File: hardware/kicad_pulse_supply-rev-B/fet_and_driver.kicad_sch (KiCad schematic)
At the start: 53 parts, among them J2 SIG_EXT, Q1 GAN7R0-150LBE, U1 UCC27611DRVT, U4 MAX4378, U6 MCP1703T-5002E/MB

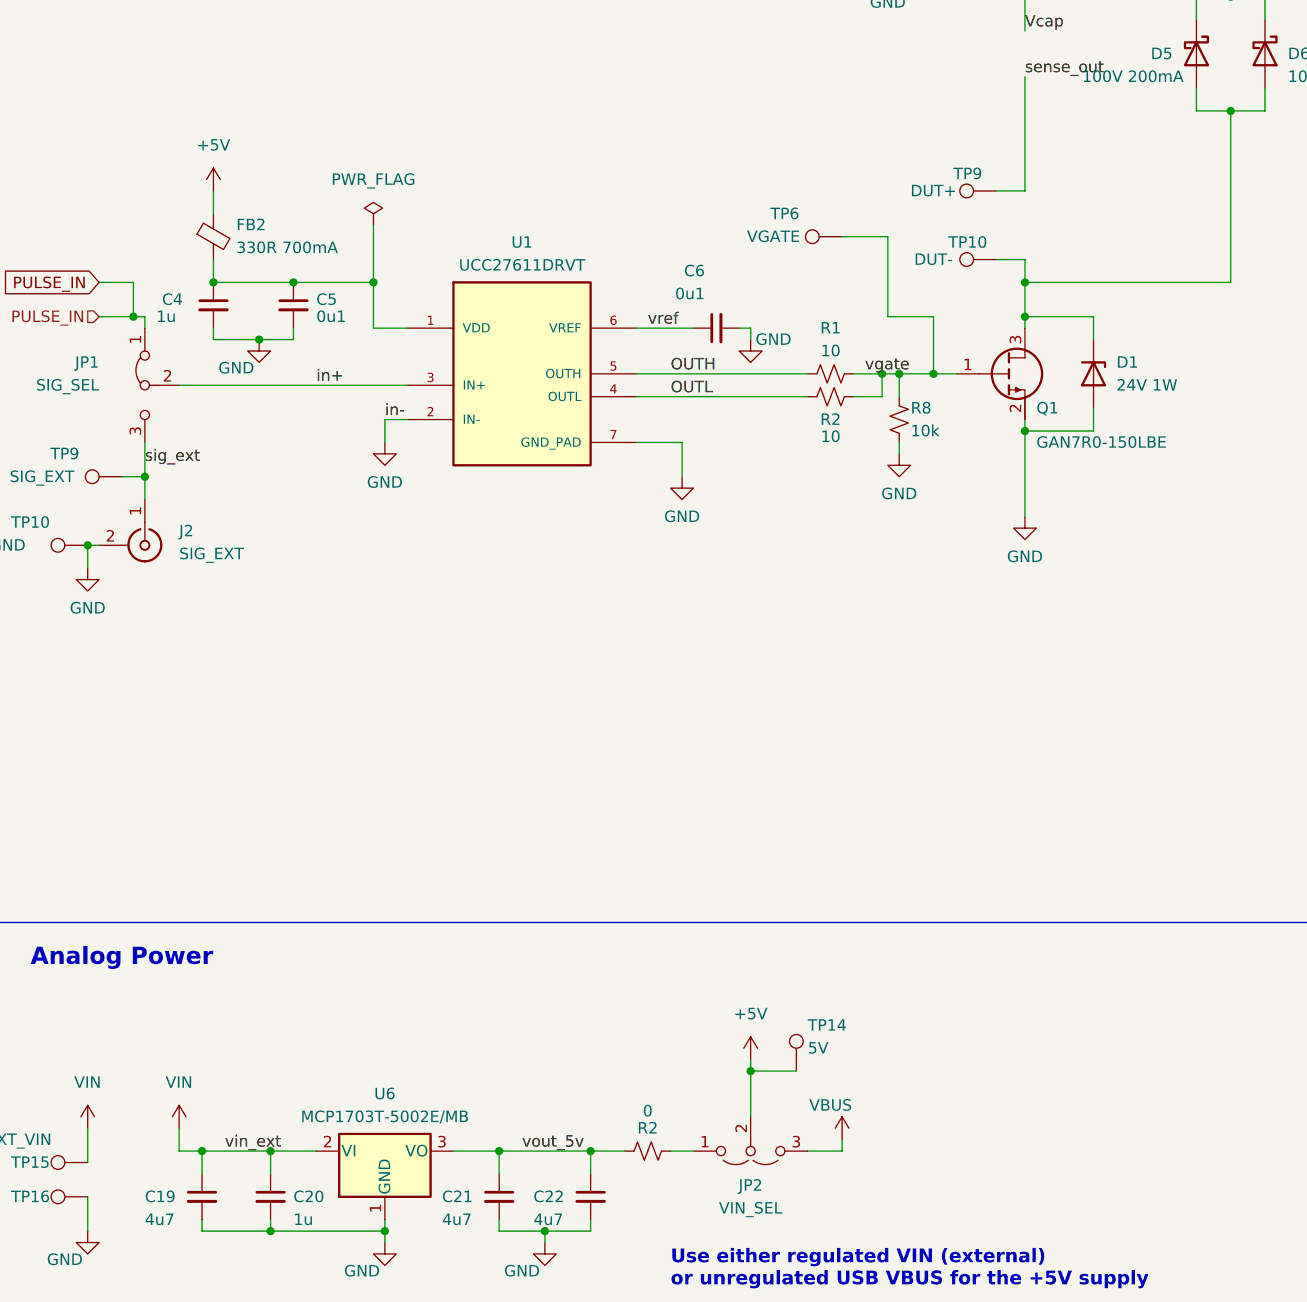
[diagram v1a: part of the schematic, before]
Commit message: Working on TPS55289 boost issues
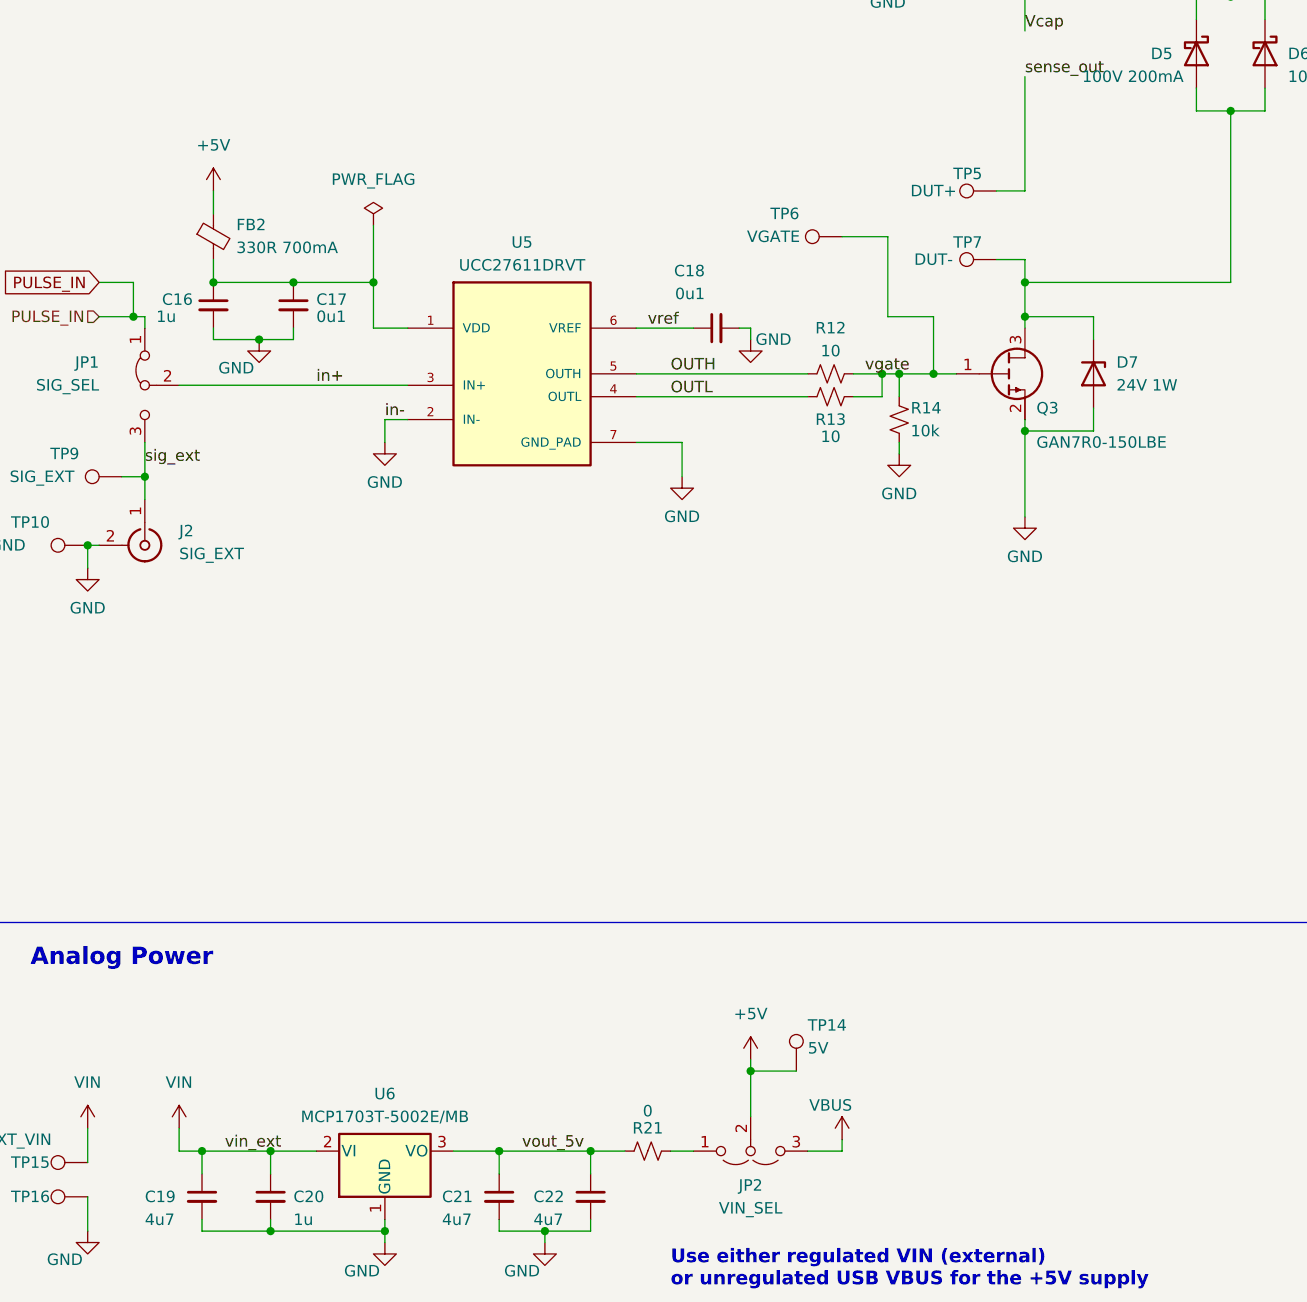
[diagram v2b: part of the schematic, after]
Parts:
- renumbered C4 to C16, C5 to C17, C6 to C18, D1 to D7, Q1 to Q3, R1 to R12, R2 to R13, R8 to R14, R2 to R21, TP9 to TP5, TP10 to TP7, U1 to U5
